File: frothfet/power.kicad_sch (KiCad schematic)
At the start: 38 parts, among them J1 Screw_Terminal_01x08, J2 Screw_Terminal_01x08, U26 TPS7A2033PDBVR, U27 MCP3425A0T-ECH, U28 XL1509-5.0

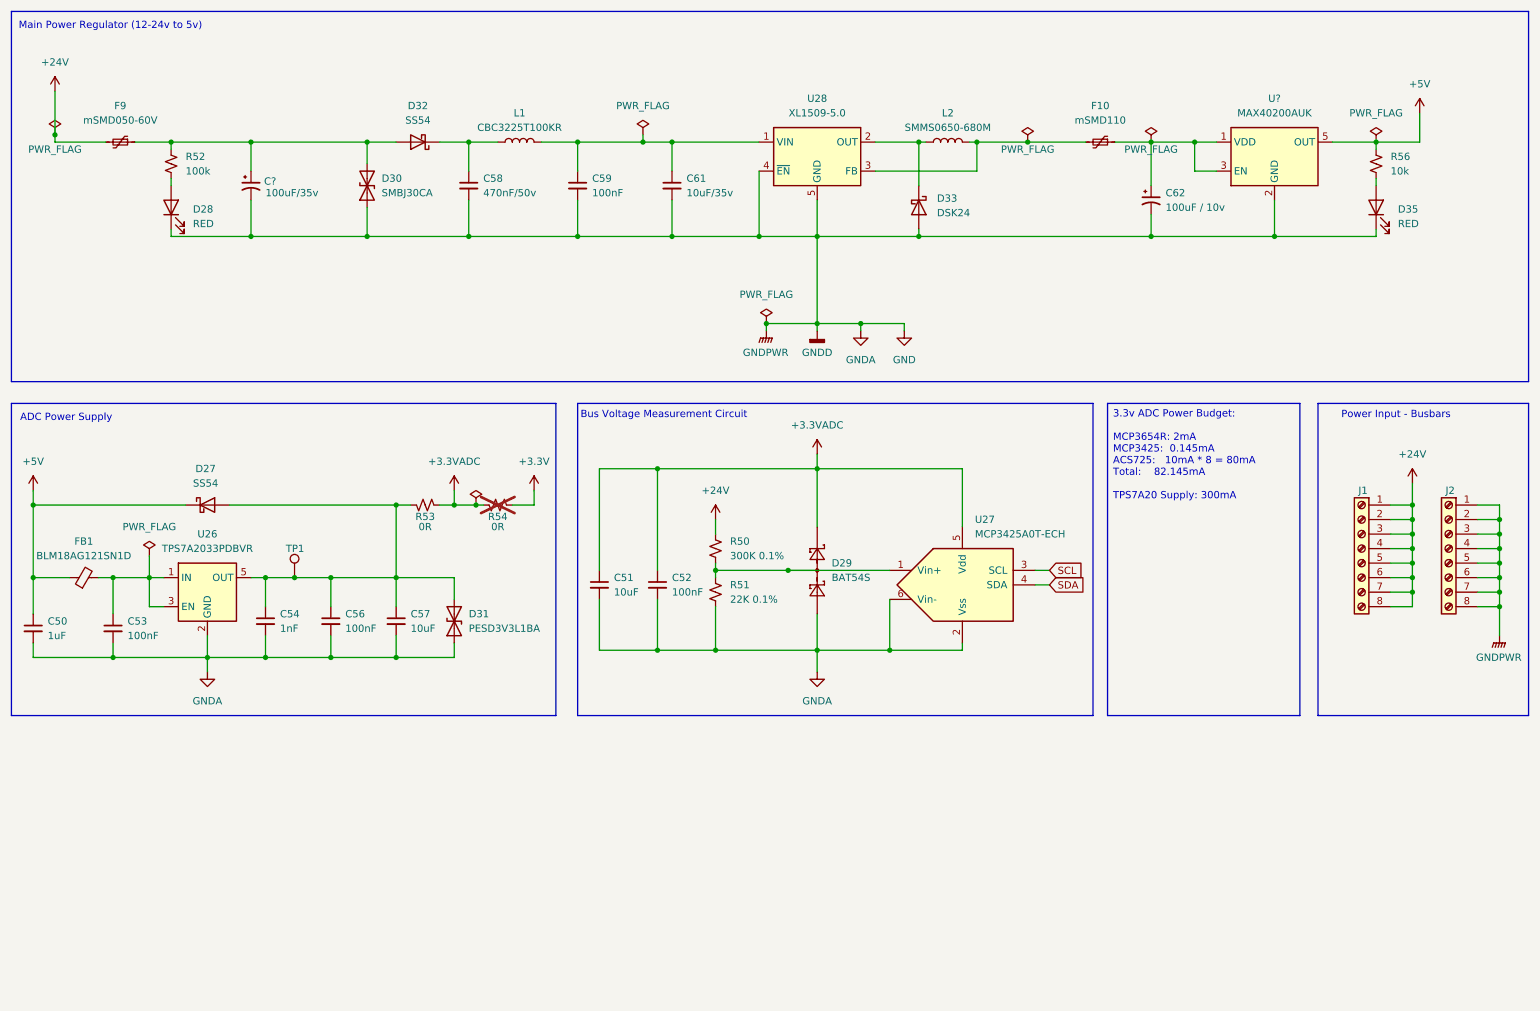
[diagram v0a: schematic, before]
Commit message: changed to a single ground
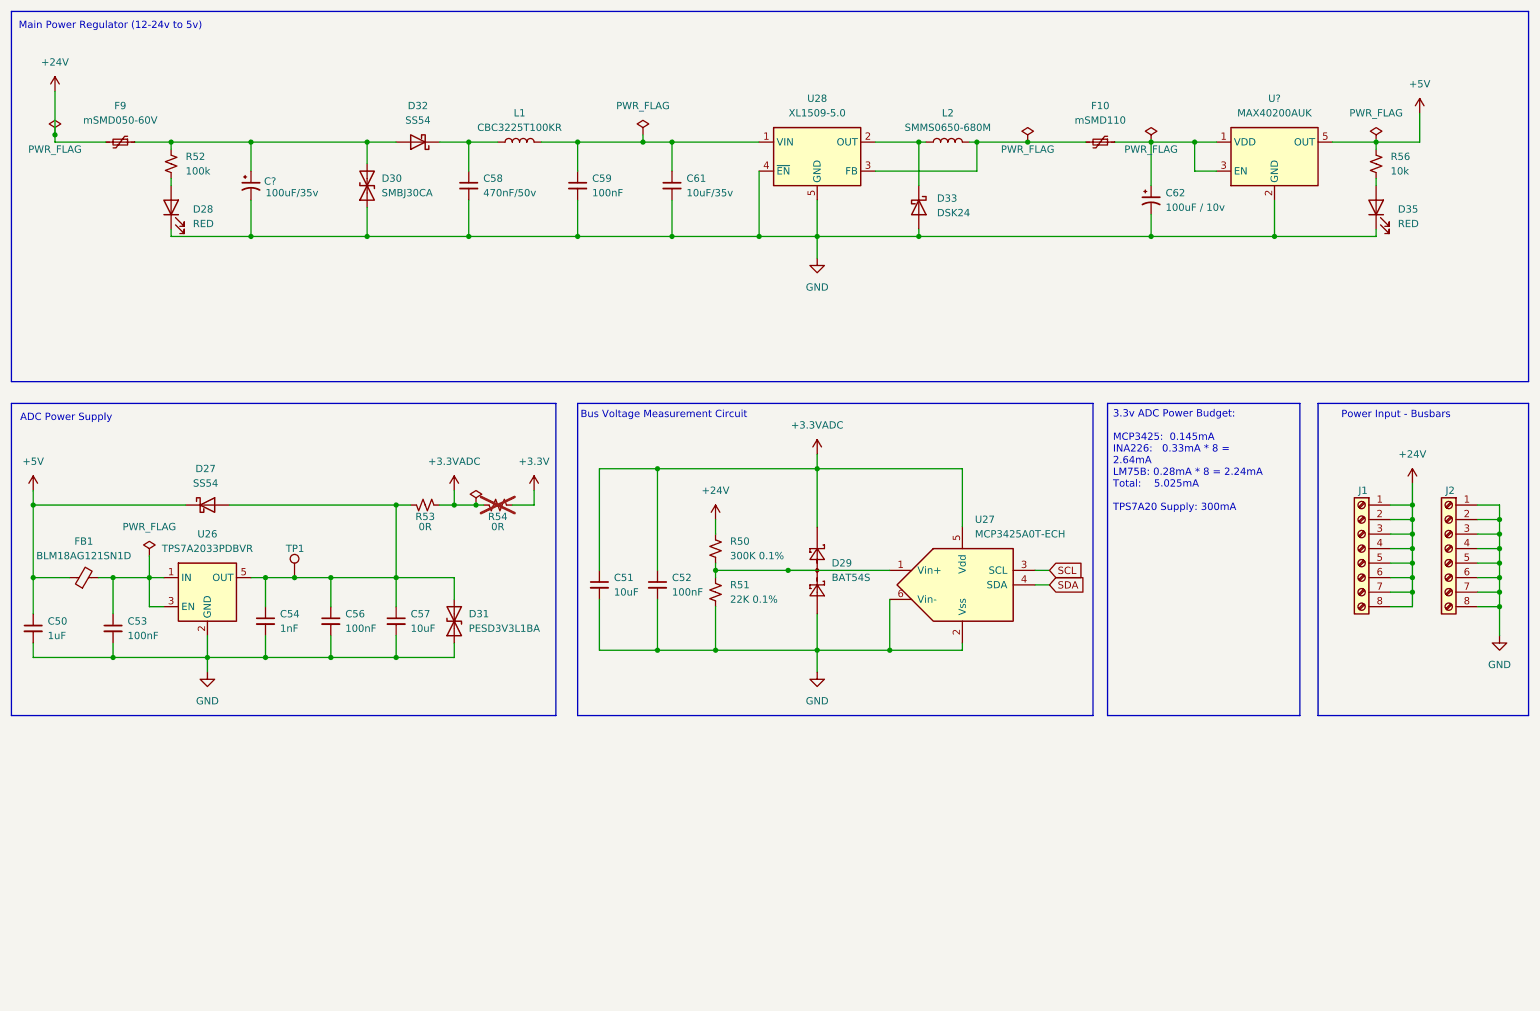
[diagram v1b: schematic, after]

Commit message: added test points
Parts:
- added TP20, TP22, TP23, TP24, TP25: ~, TestPoint:TestPoint_THTPad_D1.5mm_Drill0.7mm, symbol Connector:TestPoint
- TP19: renamed from TP1; footprint TestPoint:TestPoint_THTPad_D2.0mm_Drill1.0mm -> TestPoint:TestPoint_THTPad_D1.5mm_Drill0.7mm
- gave numbers to parts that had none: 2
- renumbered C53 to C51, C54 to C53, C56 to C54, C57 to C55, C58 to C56, C59 to C57, C51 to C58, C52 to C59, C61 to C60, C62 to C61, D28 to D27, D27 to D28, D30 to D29, D32 to D30, D29 to D32, D35 to D34, R52 to R42, R53 to R43, R54 to R44, R50 to R45, R51 to R46, R56 to R47, U28 to U27, U27 to U28
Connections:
- net +5V: now also TP25.1
- net GND: now also TP23.1
- net at C52.1, D29.2 (A2), D30.2 (A)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: now also TP20.1
- net at C57.1, C60.1, L1.2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: now also TP22.1
- net at F10.2, L2.2, U27.3 (FB): now also TP24.1

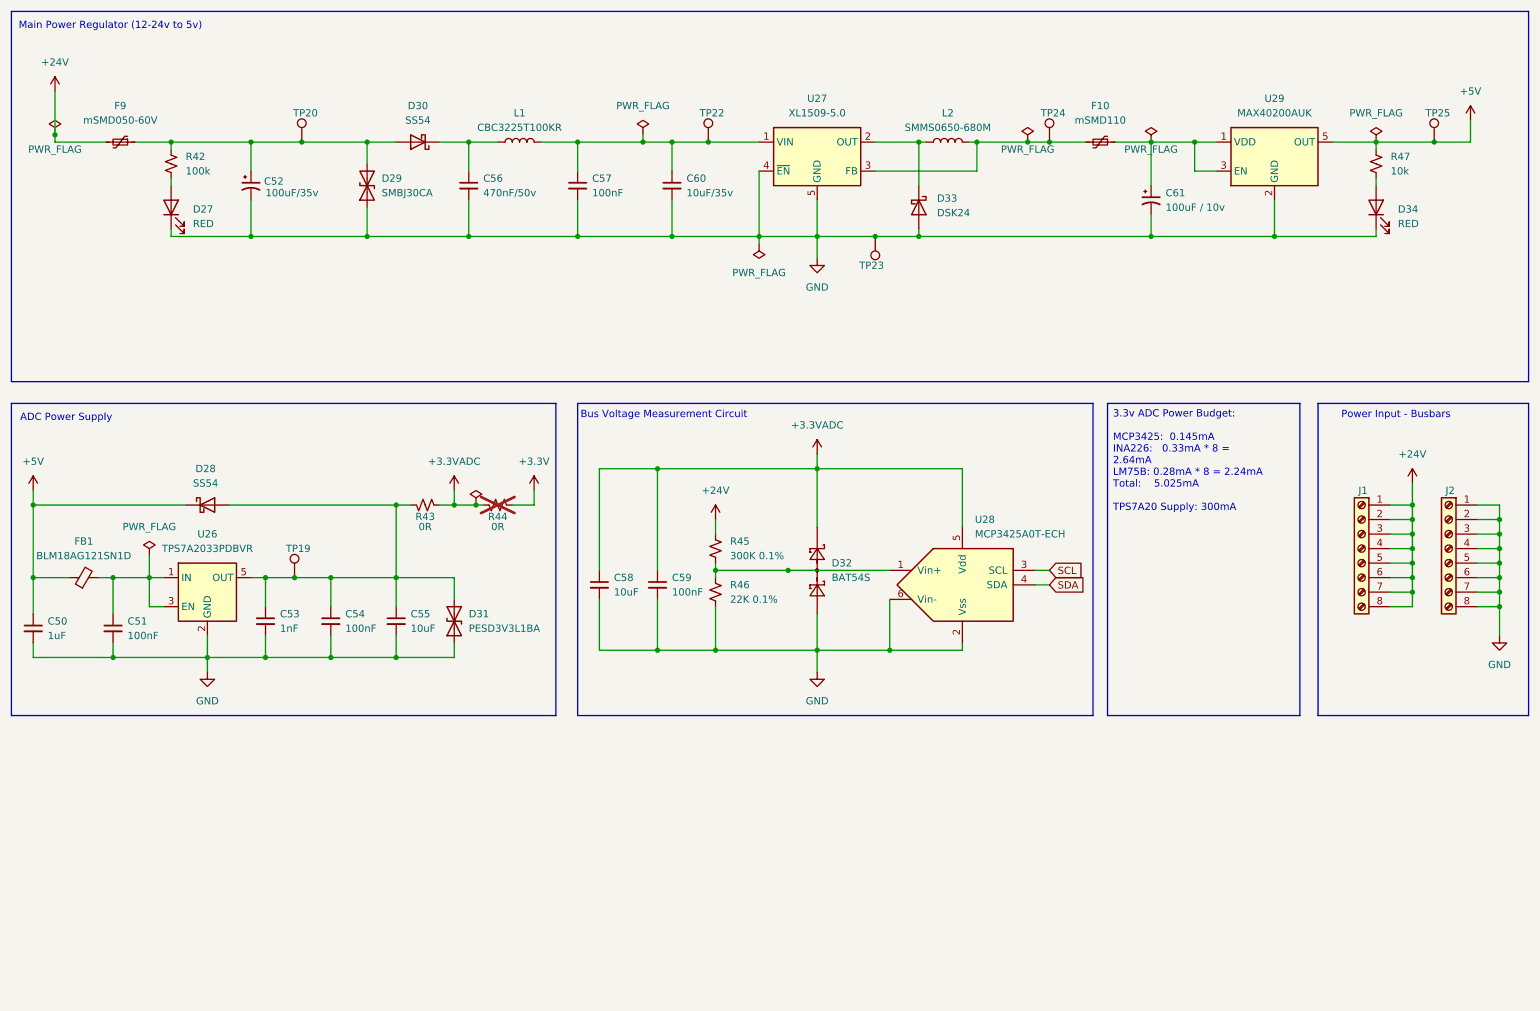
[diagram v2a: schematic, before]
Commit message: worked on routing load channel.
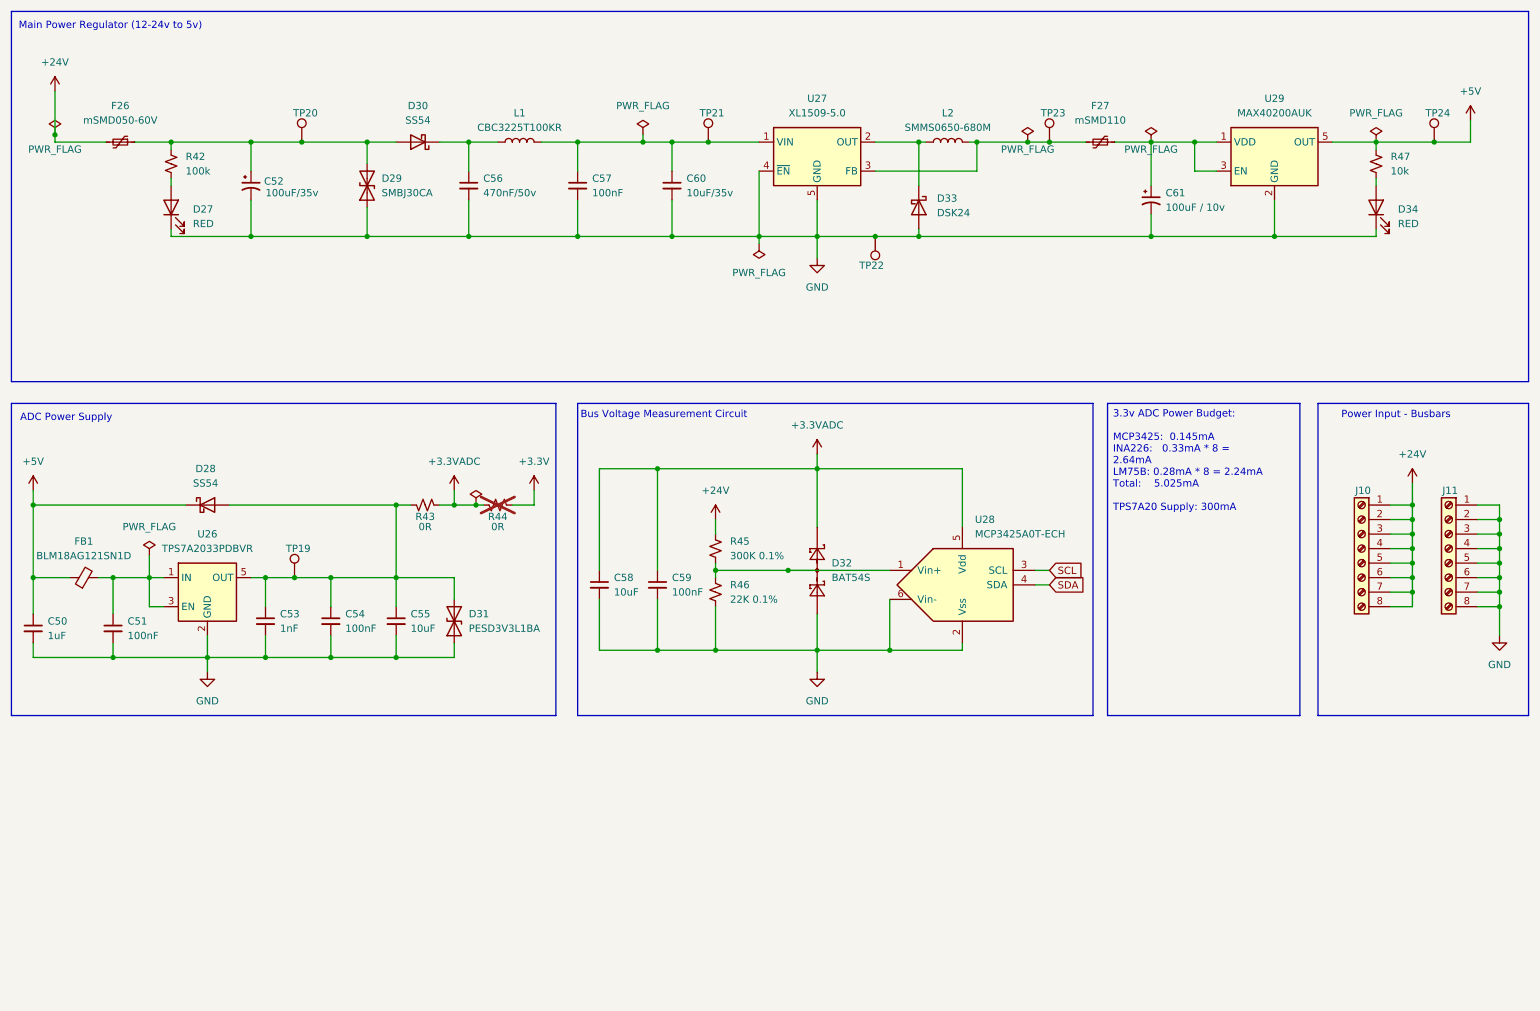
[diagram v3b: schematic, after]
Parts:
- renumbered F9 to F26, F10 to F27, J1 to J10, J2 to J11, TP22 to TP21, TP23 to TP22, TP24 to TP23, TP25 to TP24
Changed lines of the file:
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@@
 		(title "FrothFET 8CH")
 		(date "2024-08-21")
-		(rev "E")
+		(rev "F")
 		(company "https://github.com/hoeken/frothfet")
 	)
@@
 		(on_board yes)
 		(dnp no)
-		(property "Reference" "J1"
+		(property "Reference" "J10"
 			(at 251.714 99.06 0)
 			(effects
@@
 			(project ""
 				(path "/c83c6236-96e9-46ad-9d7a-9e2efa4a7966/e112a34f-fd2f-43cb-bf5d-a7f5e57b6bef"
-					(reference "J1")
+					(reference "J10")
 					(unit 1)
 				)
@@
 		(dnp no)
 		(fields_autoplaced yes)
-		(property "Reference" "#FLG07"
+		(property "Reference" "#FLG08"
 			(at 254 36.195 0)
 			(effects
@@
 			(project "8ch-mosfet"
 				(path "/c83c6236-96e9-46ad-9d7a-9e2efa4a7966/e112a34f-fd2f-43cb-bf5d-a7f5e57b6bef"
-					(reference "#FLG07")
+					(reference "#FLG08")
 					(unit 1)
 				)
@@
 		(dnp no)
 		(fields_autoplaced yes)
-		(property "Reference" "#PWR0120"
+		(property "Reference" "#PWR0125"
 			(at 19.05 102.87 0)
 			(effects
@@
 			(project "frothfet"
 				(path "/c83c6236-96e9-46ad-9d7a-9e2efa4a7966/e112a34f-fd2f-43cb-bf5d-a7f5e57b6bef"
-					(reference "#PWR0120")
+					(reference "#PWR0125")
 					(unit 1)
 				)
@@
 		(on_board yes)
 		(dnp no)
-		(property "Reference" "#FLG05"
+		(property "Reference" "#FLG06"
 			(at 193.04 36.195 0)
 			(effects
@@
 			(project "8ch-mosfet"
 				(path "/c83c6236-96e9-46ad-9d7a-9e2efa4a7966/e112a34f-fd2f-43cb-bf5d-a7f5e57b6bef"
-					(reference "#FLG05")
+					(reference "#FLG06")
 					(unit 1)
 				)
@@
 		(dnp no)
 		(fields_autoplaced yes)
-		(property "Reference" "#PWR0124"
+		(property "Reference" "#PWR0129"
 			(at 106.68 102.87 0)
 			(effects
@@
 			(project "frothfet"
 				(path "/c83c6236-96e9-46ad-9d7a-9e2efa4a7966/e112a34f-fd2f-43cb-bf5d-a7f5e57b6bef"
-					(reference "#PWR0124")
+					(reference "#PWR0129")
 					(unit 1)
 				)
@@
 		(dnp no)
 		(fields_autoplaced yes)
-		(property "Reference" "#PWR0128"
+		(property "Reference" "#PWR0133"
 			(at 156.21 137.16 0)
 			(effects
@@
 			(project "frothfet"
 				(path "/c83c6236-96e9-46ad-9d7a-9e2efa4a7966/e112a34f-fd2f-43cb-bf5d-a7f5e57b6bef"
-					(reference "#PWR0128")
+					(reference "#PWR0133")
 					(unit 1)
 				)
@@
 		(dnp no)
 		(fields_autoplaced yes)
-		(property "Reference" "#PWR0123"
+		(property "Reference" "#PWR0128"
 			(at 88.9 100.33 0)
 			(effects
@@
 			(project ""
 				(path "/c83c6236-96e9-46ad-9d7a-9e2efa4a7966/e112a34f-fd2f-43cb-bf5d-a7f5e57b6bef"
-					(reference "#PWR0123")
+					(reference "#PWR0128")
 					(unit 1)
 				)
@@
 		(on_board yes)
 		(dnp no)
-		(property "Reference" "J2"
+		(property "Reference" "J11"
 			(at 266.954 99.06 0)
 			(effects
@@
 			(project ""
 				(path "/c83c6236-96e9-46ad-9d7a-9e2efa4a7966/e112a34f-fd2f-43cb-bf5d-a7f5e57b6bef"
-					(reference "J2")
+					(reference "J11")
 					(unit 1)
 				)
@@
 		(on_board yes)
 		(dnp no)
-		(property "Reference" "TP23"
+		(property "Reference" "TP22"
 			(at 167.894 59.69 0)
 			(effects
@@
 			(project "frothfet"
 				(path "/c83c6236-96e9-46ad-9d7a-9e2efa4a7966/e112a34f-fd2f-43cb-bf5d-a7f5e57b6bef"
-					(reference "TP23")
+					(reference "TP22")
 					(unit 1)
 				)
@@
 		(dnp no)
 		(fields_autoplaced yes)
-		(property "Reference" "#PWR0125"
+		(property "Reference" "#PWR0130"
 			(at 138.43 107.95 0)
 			(effects
@@
 			(project "8ch-mosfet"
 				(path "/c83c6236-96e9-46ad-9d7a-9e2efa4a7966/e112a34f-fd2f-43cb-bf5d-a7f5e57b6bef"
-					(reference "#PWR0125")
+					(reference "#PWR0130")
 					(unit 1)
 				)
@@
 		(on_board yes)
 		(dnp no)
-		(property "Reference" "TP24"
+		(property "Reference" "TP23"
 			(at 195.326 33.02 0)
 			(effects
@@
 			(project "frothfet"
 				(path "/c83c6236-96e9-46ad-9d7a-9e2efa4a7966/e112a34f-fd2f-43cb-bf5d-a7f5e57b6bef"
-					(reference "TP24")
+					(reference "TP23")
 					(unit 1)
 				)
@@
 		(on_board yes)
 		(dnp no)
-		(property "Reference" "TP25"
+		(property "Reference" "TP24"
 			(at 262.636 33.02 0)
 			(effects
@@
 			(project "frothfet"
 				(path "/c83c6236-96e9-46ad-9d7a-9e2efa4a7966/e112a34f-fd2f-43cb-bf5d-a7f5e57b6bef"
-					(reference "TP25")
+					(reference "TP24")
 					(unit 1)
 				)
@@
 		(dnp no)
 		(fields_autoplaced yes)
-		(property "Reference" "F10"
+		(property "Reference" "F27"
 			(at 205.74 31.75 90)
 			(effects
@@
 			(project "8ch-mosfet"
 				(path "/c83c6236-96e9-46ad-9d7a-9e2efa4a7966/e112a34f-fd2f-43cb-bf5d-a7f5e57b6bef"
-					(reference "F10")
+					(reference "F27")
 					(unit 1)
 				)
@@
 		(dnp no)
 		(fields_autoplaced yes)
-		(property "Reference" "#PWR0131"
+		(property "Reference" "#PWR0136"
 			(at 275.59 130.81 0)
 			(effects
@@
 			(project "8ch-mosfet"
 				(path "/c83c6236-96e9-46ad-9d7a-9e2efa4a7966/e112a34f-fd2f-43cb-bf5d-a7f5e57b6bef"
-					(reference "#PWR0131")
+					(reference "#PWR0136")
 					(unit 1)
 				)
@@
 		(dnp no)
 		(fields_autoplaced yes)
-		(property "Reference" "#PWR0129"
+		(property "Reference" "#PWR0134"
 			(at 260.35 101.6 0)
 			(effects
@@
 			(project "8ch-mosfet"
 				(path "/c83c6236-96e9-46ad-9d7a-9e2efa4a7966/e112a34f-fd2f-43cb-bf5d-a7f5e57b6bef"
-					(reference "#PWR0129")
+					(reference "#PWR0134")
 					(unit 1)
 				)
@@
 		(dnp no)
 		(fields_autoplaced yes)
-		(property "Reference" "F9"
+		(property "Reference" "F26"
 			(at 34.29 31.75 90)
 			(effects
@@
 			(project "8ch-mosfet"
 				(path "/c83c6236-96e9-46ad-9d7a-9e2efa4a7966/e112a34f-fd2f-43cb-bf5d-a7f5e57b6bef"
-					(reference "F9")
+					(reference "F26")
 					(unit 1)
 				)
@@
 		(dnp no)
 		(fields_autoplaced yes)
-		(property "Reference" "#PWR0126"
+		(property "Reference" "#PWR0131"
 			(at 156.21 64.77 0)
 			(effects
@@
 			(project "8ch-mosfet"
 				(path "/c83c6236-96e9-46ad-9d7a-9e2efa4a7966/e112a34f-fd2f-43cb-bf5d-a7f5e57b6bef"
-					(reference "#PWR0126")
+					(reference "#PWR0131")
 					(unit 1)
 				)
@@
 		(dnp no)
 		(fields_autoplaced yes)
-		(property "Reference" "#PWR0130"
+		(property "Reference" "#PWR0135"
 			(at 270.51 38.1 0)
 			(effects
@@
 			(project "8ch-mosfet"
 				(path "/c83c6236-96e9-46ad-9d7a-9e2efa4a7966/e112a34f-fd2f-43cb-bf5d-a7f5e57b6bef"
-					(reference "#PWR0130")
+					(reference "#PWR0135")
 					(unit 1)
 				)
@@
 		(dnp no)
 		(fields_autoplaced yes)
-		(property "Reference" "#PWR0122"
+		(property "Reference" "#PWR0127"
 			(at 49.53 137.16 0)
 			(effects
@@
 			(project ""
 				(path "/c83c6236-96e9-46ad-9d7a-9e2efa4a7966/e112a34f-fd2f-43cb-bf5d-a7f5e57b6bef"
-					(reference "#PWR0122")
+					(reference "#PWR0127")
 					(unit 1)
 				)
@@
 		(dnp no)
 		(fields_autoplaced yes)
-		(property "Reference" "#PWR0121"
+		(property "Reference" "#PWR0126"
 			(at 22.86 33.02 0)
 			(effects
@@
 			(project "8ch-mosfet"
 				(path "/c83c6236-96e9-46ad-9d7a-9e2efa4a7966/e112a34f-fd2f-43cb-bf5d-a7f5e57b6bef"
-					(reference "#PWR0121")
+					(reference "#PWR0126")
 					(unit 1)
 				)
@@
 		(on_board yes)
 		(dnp no)
-		(property "Reference" "#FLG06"
+		(property "Reference" "#FLG07"
 			(at 214.63 36.195 0)
 			(effects
@@
 			(project "8ch-mosfet"
 				(path "/c83c6236-96e9-46ad-9d7a-9e2efa4a7966/e112a34f-fd2f-43cb-bf5d-a7f5e57b6bef"
-					(reference "#FLG06")
+					(reference "#FLG07")
 					(unit 1)
 				)
@@
 		(on_board yes)
 		(dnp no)
-		(property "Reference" "TP22"
+		(property "Reference" "TP21"
 			(at 135.636 33.02 0)
 			(effects
@@
 			(project "frothfet"
 				(path "/c83c6236-96e9-46ad-9d7a-9e2efa4a7966/e112a34f-fd2f-43cb-bf5d-a7f5e57b6bef"
-					(reference "TP22")
+					(reference "TP21")
 					(unit 1)
 				)
@@
 		(dnp no)
 		(fields_autoplaced yes)
-		(property "Reference" "#PWR0127"
+		(property "Reference" "#PWR0132"
 			(at 160.02 93.98 0)
 			(effects
@@
 			(project "frothfet"
 				(path "/c83c6236-96e9-46ad-9d7a-9e2efa4a7966/e112a34f-fd2f-43cb-bf5d-a7f5e57b6bef"
-					(reference "#PWR0127")
+					(reference "#PWR0132")
 					(unit 1)
 				)
@@
 		(dnp no)
 		(fields_autoplaced yes)
-		(property "Reference" "#FLG010"
+		(property "Reference" "#FLG05"
 			(at 146.05 57.785 0)
 			(effects
@@
 			(project "frothfet"
 				(path "/c83c6236-96e9-46ad-9d7a-9e2efa4a7966/e112a34f-fd2f-43cb-bf5d-a7f5e57b6bef"
-					(reference "#FLG010")
+					(reference "#FLG05")
 					(unit 1)
 				)
